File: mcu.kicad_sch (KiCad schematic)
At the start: 13 parts, among them U6 ATtiny3217

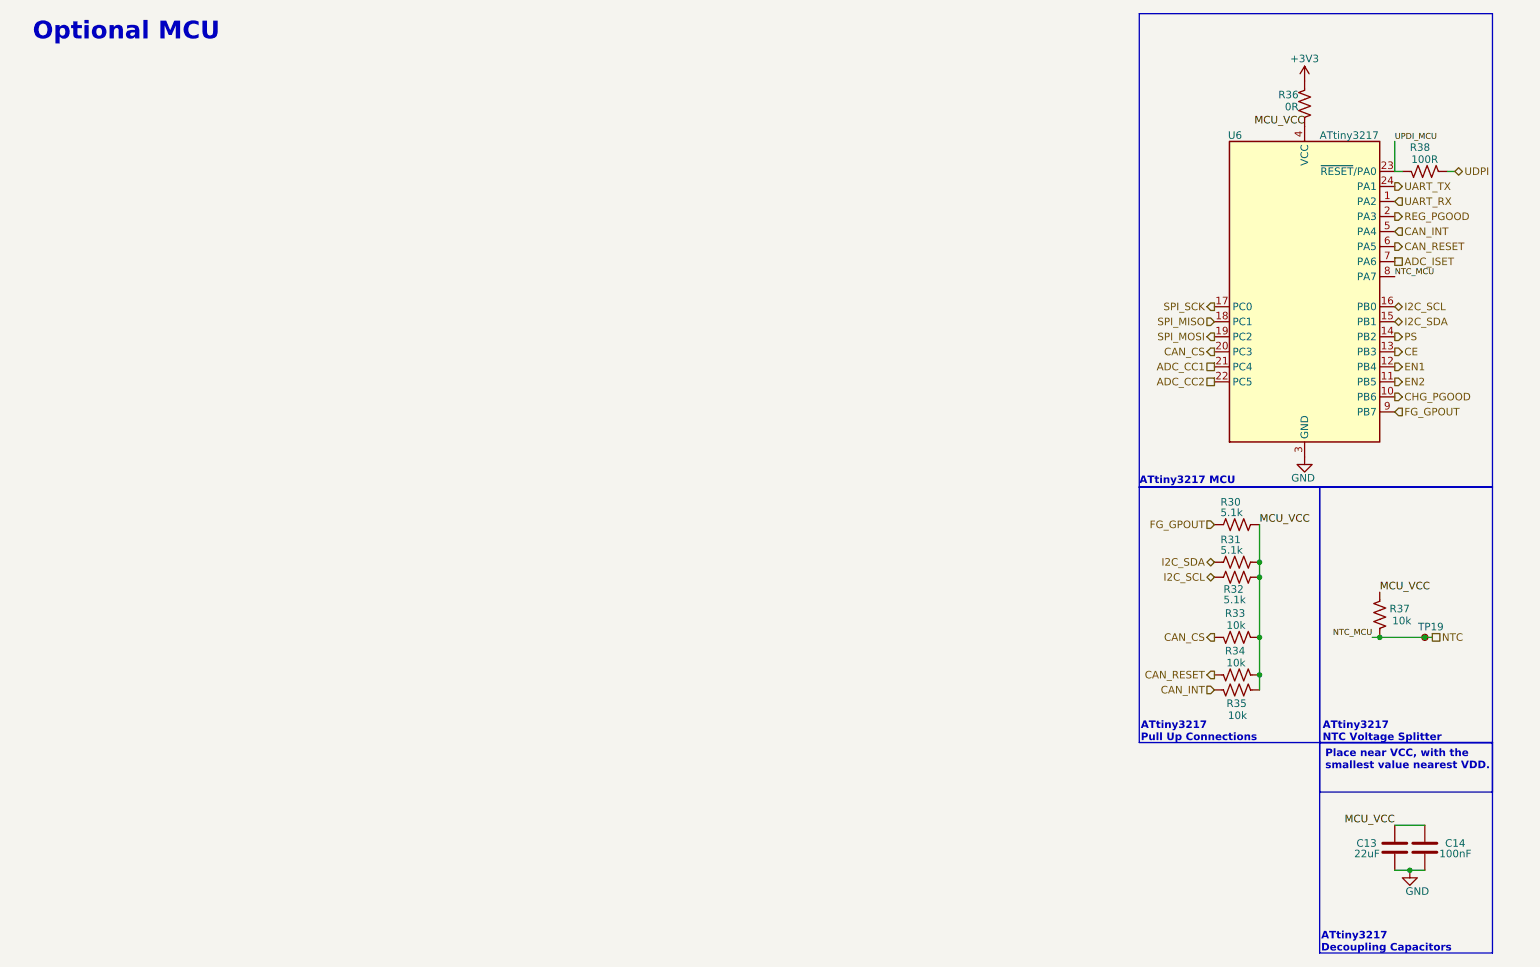
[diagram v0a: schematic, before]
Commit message: Added Graph & cleaned up title and layout
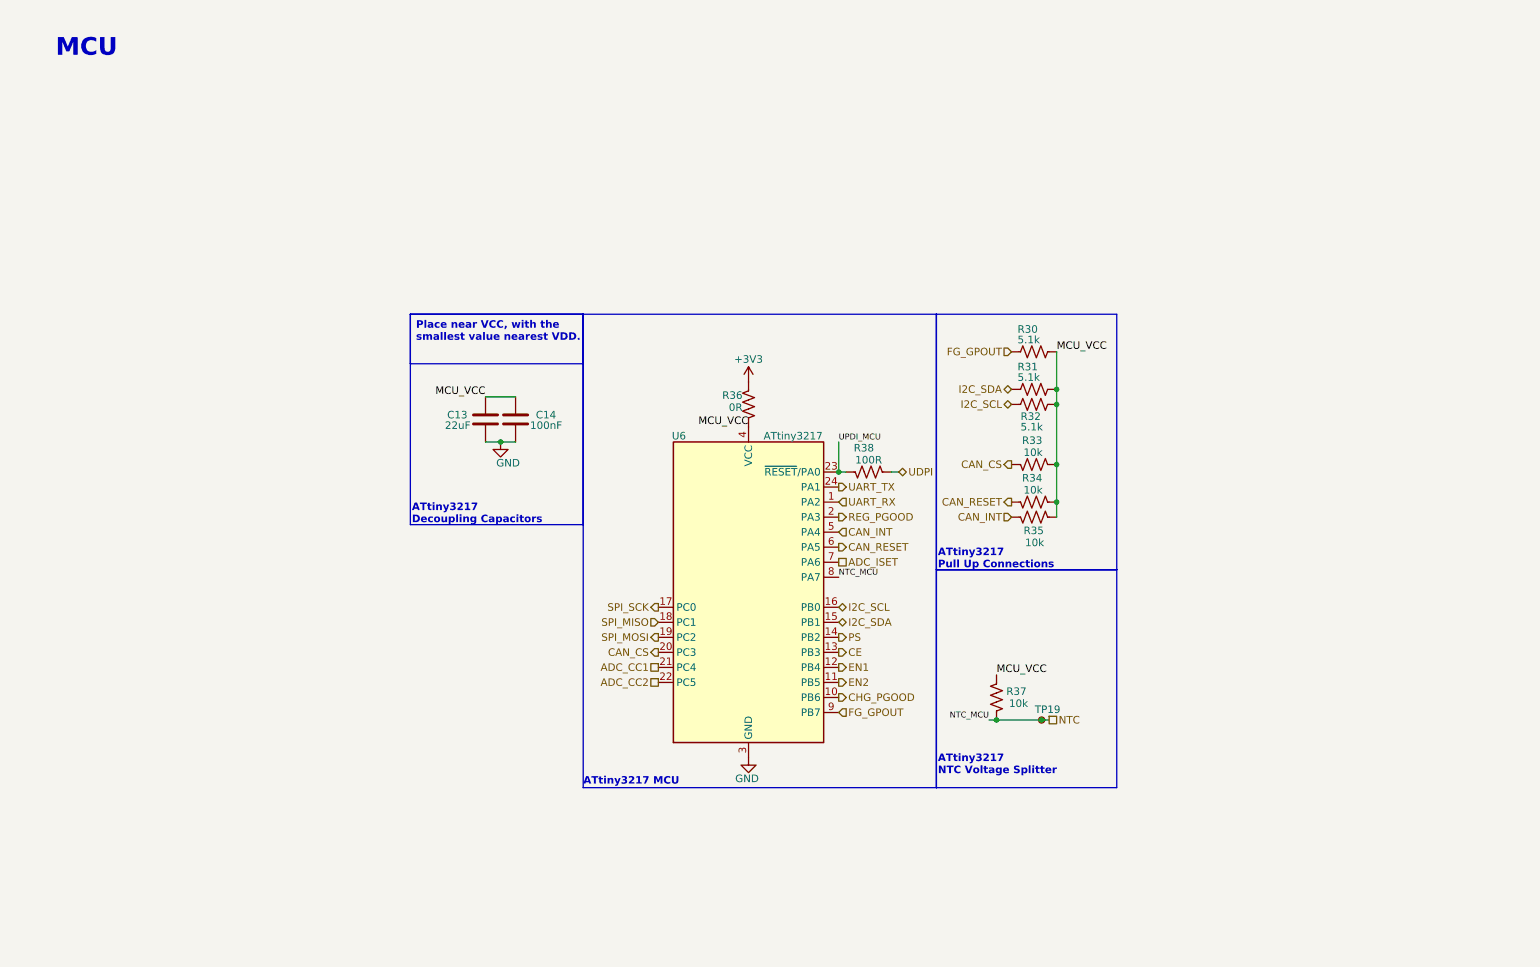
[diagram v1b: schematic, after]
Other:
- note added: "MCU"
- note removed: "Optional MCU"
- company: FETfox -> github.com/FETfox/Li-Ion_Power_Module
- title: Li Lion Power Module -> Li Lion Power Module w/ Optional Fuel Gauge &CAN Bus
- moved on the sheet: C13, C14, R30, R31, R32, R33, R34, R35, R36, R37, R38, TP19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
